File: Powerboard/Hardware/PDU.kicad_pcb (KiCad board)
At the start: 4 copper layers, 58 x 50 mm, 148 parts, among them IC1 TPS259830ONRGER, IC2 SiC437AED-T1-GE3, J1 Conn_01x03_MountingPin, J2 FAN, J3 USB_C_Receptacle_USB2.0, J4 Conn_01x02_Male, J5 Conn_01x08_Male, J6 Conn_01x02_Male, J7 XT60PW-M, J8 Conn_01x04_Male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

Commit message: changes post 3rd review
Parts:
- J1: footprint iclr:Molex_Nano-Fit_105313-xx02_1x02_P2.50mm_Horizontal -> Connector_Molex:Molex_Nano-Fit_105313-xx02_1x02_P2.50mm_Horizontal

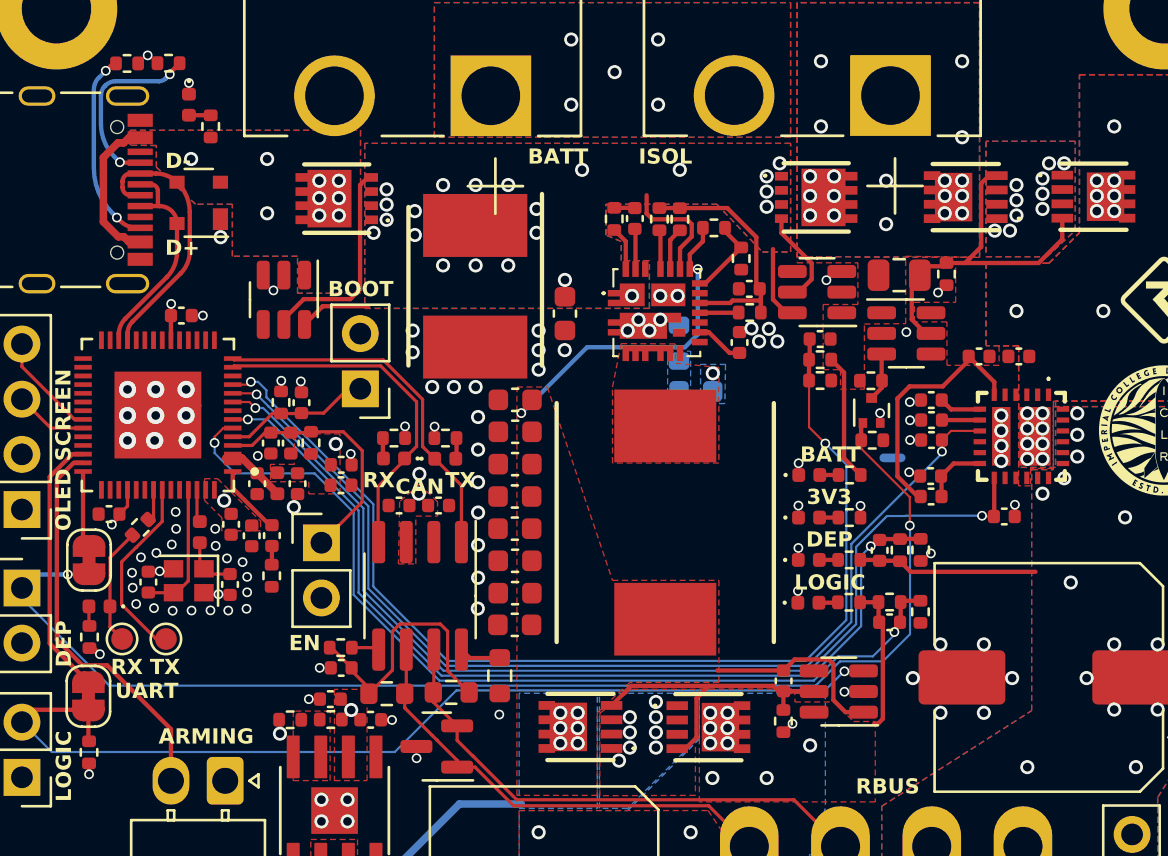
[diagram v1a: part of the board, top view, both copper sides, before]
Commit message: esp32 adc cap was in wrong place
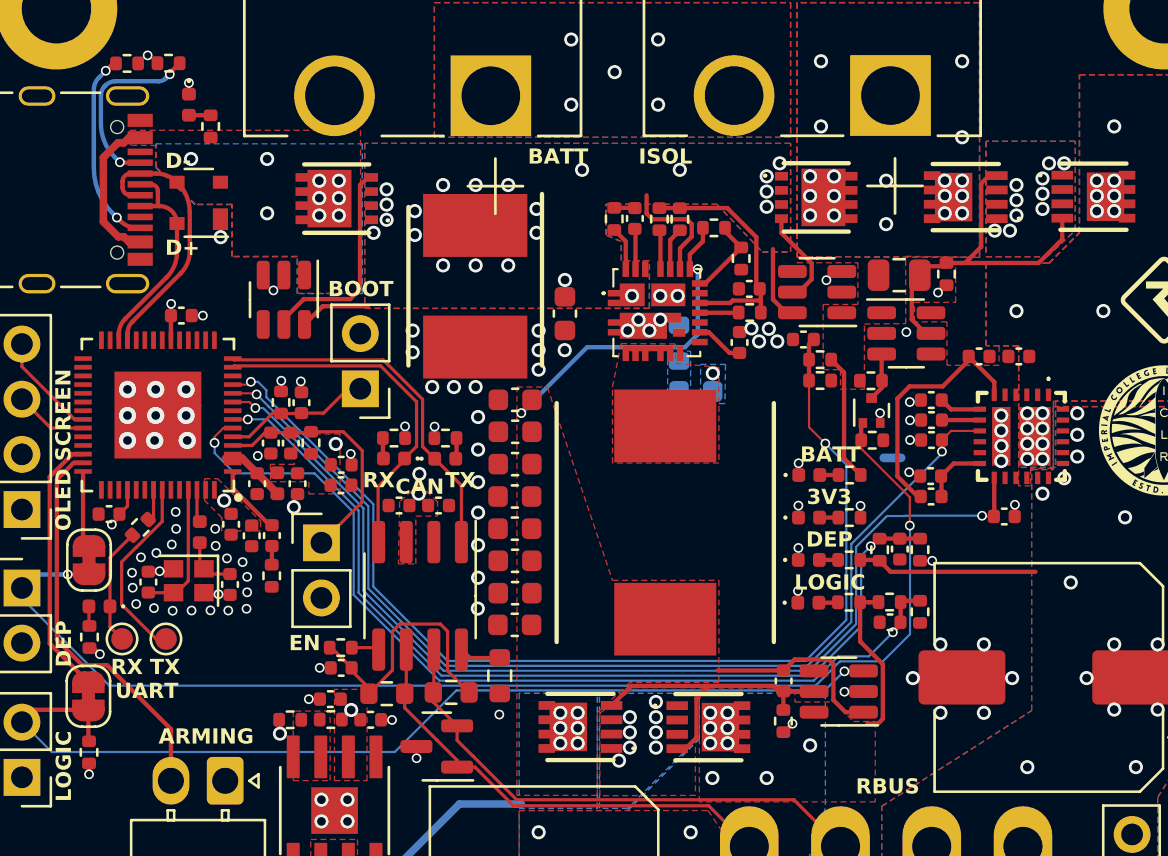
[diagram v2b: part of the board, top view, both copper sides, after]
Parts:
- moved R28 0.94 mm to (153.7, 100.5)
- moved C27 0.93 mm to (154.6, 100.5), turned to -90 degrees
- moved C28 0.77 mm to (150.2, 90.9)
- turned C26 to 180 degrees
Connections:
- C26 pad 1: Net-(J5-Pin_4) -> /LogicVoltage
- C26 pad 2: /LogicVoltage -> GND
- C27 pad 1: /Switches+RBUS/EFuse_OUT -> /DepVoltage
- C27 pad 2: /DepVoltage -> GND
- C28 pad 1: +12V -> /BattVoltage
- C28 pad 2: /BattVoltage -> GND
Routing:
- net Net-(J5-Pin_4): track 6.80 -> 7.47 mm
- net /DepVoltage: track 43.3 -> 42.8 mm

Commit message: post Andrei review
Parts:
- removed C29: 2.2uF, Capacitor_SMD:C_0402_1005Metric
- removed C31: 2.2uF, Capacitor_SMD:C_0805_2012Metric
- removed R44, R45: 100k, Resistor_SMD:R_0402_1005Metric
- added D4: SMCJ24AHE3_A/H, Diode_SMD:D_SMC, F.Cu at (164.1, 88.6)
- added R46: 2.2k, Resistor_SMD:R_0402_1005Metric, F.Cu at (118.1, 91.6)
- added R47: 100k, Resistor_SMD:R_0402_1005Metric, F.Cu at (133.1, 86.3)
- C12: value DNP -> 2.2uF
- C16: value 680pF -> TBD
- R37: value 5.1 -> TBD
- R42: value 681 -> 680
- R8: value DNP -> 2.2k
- moved C17 22.3 mm to (131.4, 119.7), turned to 0 degrees
- moved C12 15.3 mm to (131.7, 85.8), turned to 0 degrees
- moved G*** 12.3 mm to (164.0, 77.1)
- moved R8 11.0 mm to (118.1, 93.8)
- moved R5 6.56 mm to (120.2, 98.7), turned to -90 degrees
- moved R23 5.00 mm to (131.6, 100.9), turned to -90 degrees
- moved U7 4.27 mm to (157.1, 86.9)
- moved R35 4.26 mm to (155.5, 89.1)
- moved C20 4.25 mm to (131.6, 102.7), turned to -90 degrees
- moved Q1 4.23 mm to (155.5, 90.5)
- moved R34 4.23 mm to (155.5, 91.8)
- moved C34 3.94 mm to (139.1, 100.8)
- moved C30 3.93 mm to (139.1, 99.3)
- moved C52 3.91 mm to (130.9, 113.9)
- moved C32 3.91 mm to (139.1, 97.8)
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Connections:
- C12 pad 1: Net-(C12-Pad1) -> VBUS
- C12 pad 2: Net-(U2-LNA_IN/RF) -> Net-(Q6-G)
- R8 pad 1: GND -> +3V3
- R8 pad 2: Net-(C12-Pad1) -> /SCL
- U2 pad 1: Net-(U2-LNA_IN/RF) -> unconnected-(U2-LNA_IN/RF-Pad1)
- U2 pad 40: /LogicSwitch -> /DepSwitch
- U2 pad 41: /ARMING -> /LogicSwitch
- U2 pad 42: /DepSwitch -> /ARMING
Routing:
- net VBUS: track 7.11 -> 0.00 mm
- net /Switches+RBUS/EFuse_IN: track 0.00 -> 6.00 mm, vias 21 -> 22
- net +12V: track 5.87 -> 11.8 mm
- net RBUS_uC_V: track 40.0 -> 45.0 mm
- net /CAN+: track 24.3 -> 28.2 mm
- net Net-(U2-LNA_IN/RF): track 3.28 -> 0.00 mm
- net Net-(J4-Pin_2): track 45.6 -> 42.6 mm, vias 1 -> 2
- net /CAN-: track 21.4 -> 24.3 mm
- net /EFuse_PG: track 49.4 -> 46.7 mm
- net /DepSwitch: track 3.54 -> 5.96 mm
- net Net-(J3-CC1): track 8.61 -> 6.20 mm
- net Net-(J3-CC2): track 9.07 -> 6.71 mm
- net /ARMING: track 18.2 -> 16.0 mm
- net Net-(IC2-EN): track 12.2 -> 14.2 mm, vias 22 -> 19
- net /DepCurrent: track 48.8 -> 46.7 mm
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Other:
- board size 58 x 50 mm -> 59 x 50 mm
- board text added: "OLED"
- board text added: "RAE 2024 Designed by Artem Sheykin"
- board text added: "x"
- board text removed: "Designed by Artem Sheykin RAE 2024"
- board text removed: "OLED SCREEN"
